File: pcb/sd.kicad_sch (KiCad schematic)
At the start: 8 parts, among them J1 Micro_SD_Card_Det2, J2 Conn_01x09

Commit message: Ready for order
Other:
- moved on the sheet: J1, J2, R1, R2, R3, R4, R5, R6

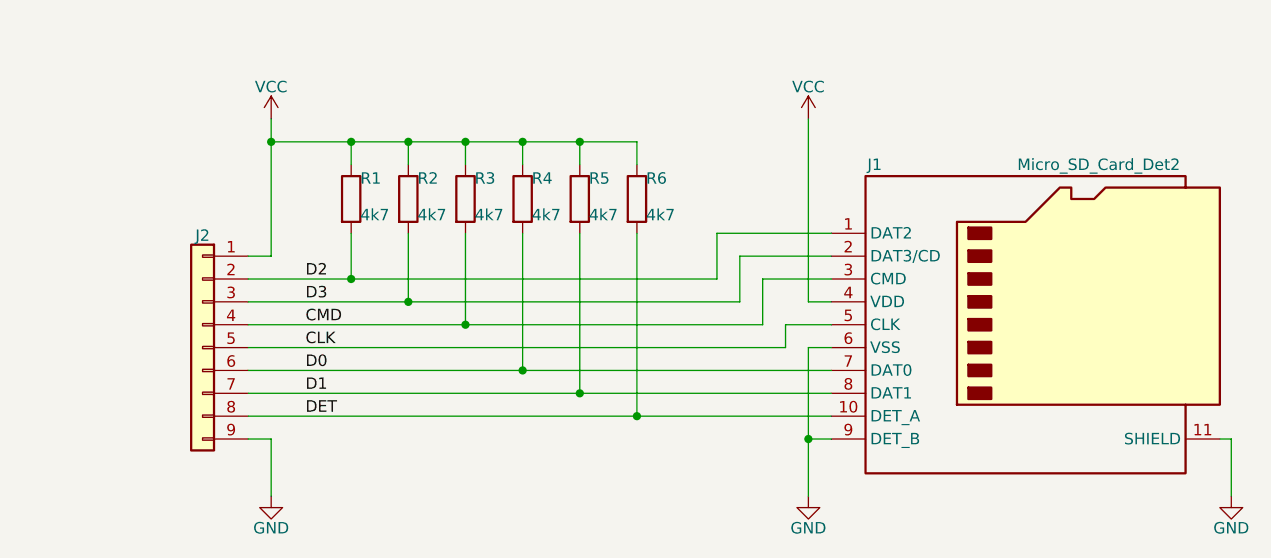
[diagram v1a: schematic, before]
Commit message: Bumped work revision to b.  Added capacitors which may or may not be needed.
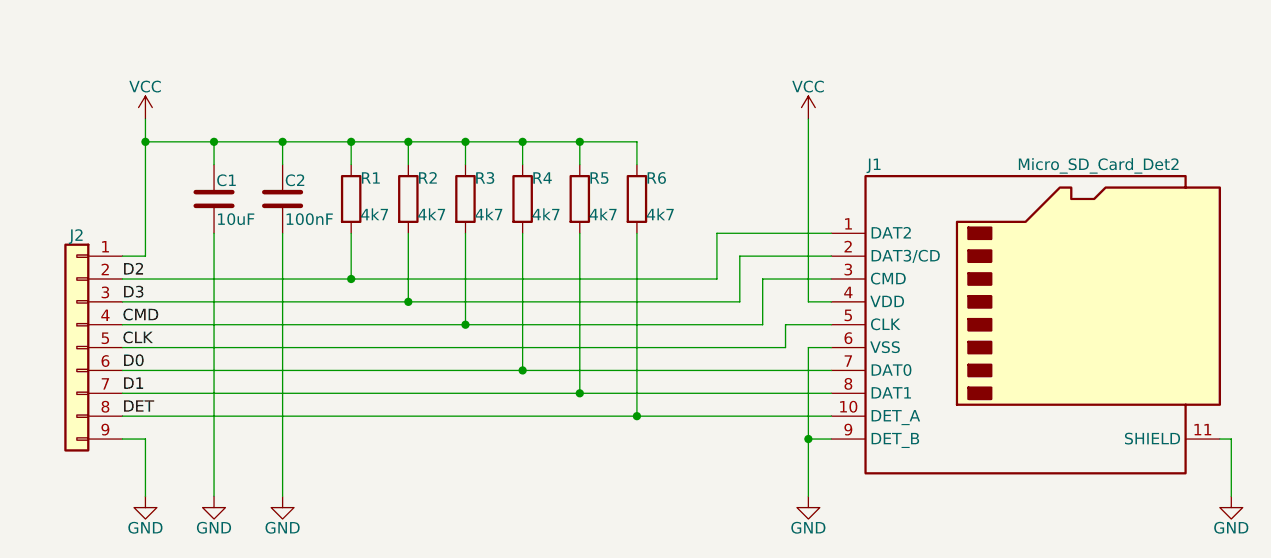
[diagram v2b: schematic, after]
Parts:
- added C1: 10uF, Capacitor_SMD:C_0603_1608Metric, symbol Device:C
- added C2: 100nF, Capacitor_SMD:C_0603_1608Metric, symbol Device:C
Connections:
- net GND: now also C1.2, C2.2
- net VCC: now also C1.1, C2.1
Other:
- moved on the sheet: J2

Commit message: Order rev_b
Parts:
- C1: LCSC C719027 -> C19702
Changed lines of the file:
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@@
 			)
 		)
-		(property "LCSC" "C719027"
+		(property "LCSC" "C19702"
 			(at 96.52 82.55 0)
 			(effects
